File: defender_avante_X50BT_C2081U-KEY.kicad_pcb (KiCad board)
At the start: 2 copper layers, 172.7 x 61 mm, 77 parts, among them CN301 CONNECTOR_M_006_20_SPECIAL, J300 JUMPER, J301 JUMPER, J302 JUMPER, J303 JUMPER, J304 JUMPER, J305 JUMPER, J306 JUMPER, J307 JUMPER, J308 JUMPER, J309 JUMPER, J310 JUMPER, J311 JUMPER, J312 JUMPER, J313 JUMPER, J314 JUMPER, J315 JUMPER, J316 JUMPER, J317 JUMPER, J318 JUMPER, J319 JUMPER, J320 JUMPER, J321 JUMPER, J322 JUMPER, J323 JUMPER, J324 JUMPER, J325 JUMPER, J326 JUMPER, J327 JUMPER, J328 JUMPER, J329 JUMPER, J330 JUMPER, J331 JUMPER, J332 JUMPER, J333 JUMPER, J334 JUMPER, J335 JUMPER, J336 JUMPER, J337 JUMPER, Q300 BJT_NPN_GENERAL, U300 IC_X2Y_TM1668

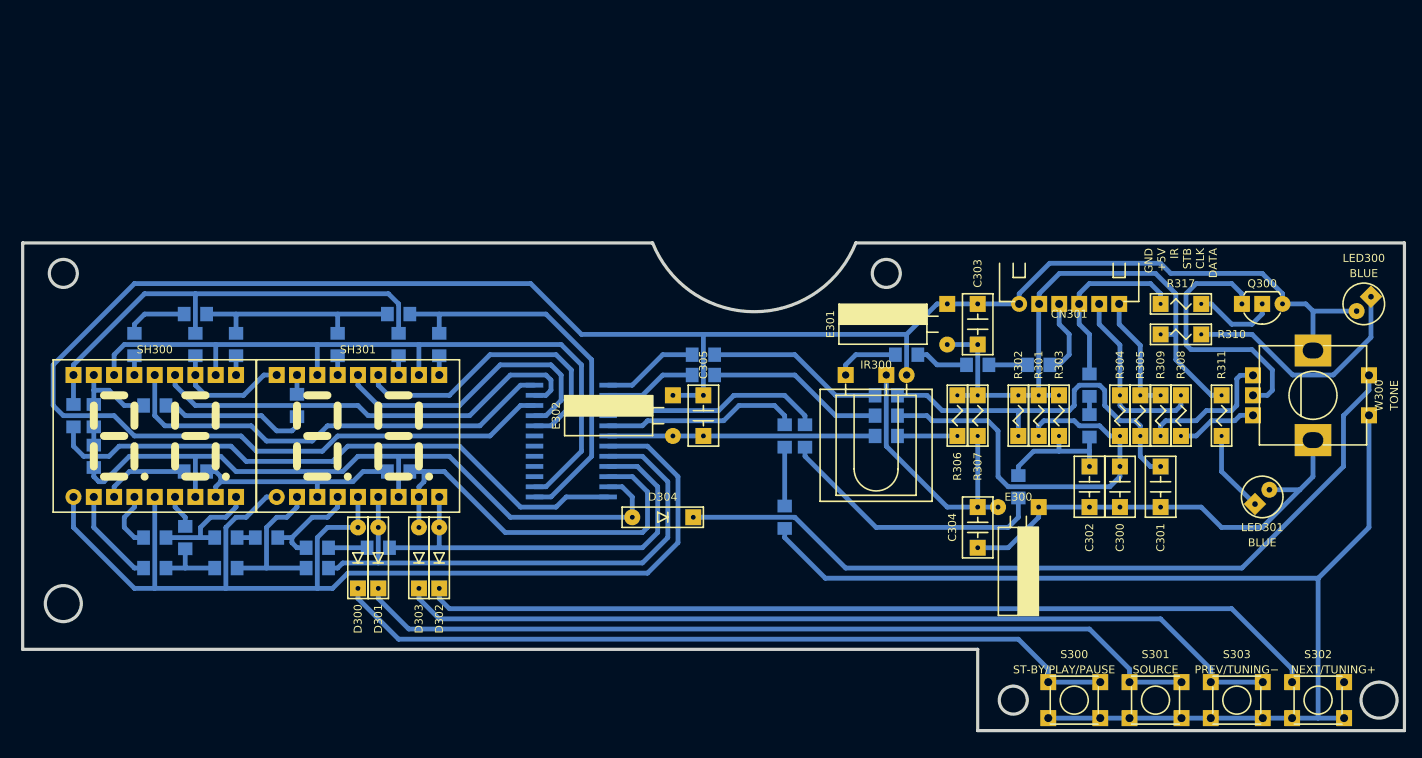
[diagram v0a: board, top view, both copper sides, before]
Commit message: Скорректированы размеры платы, положение монтажных отверстий, кнопок, энкодера и светодиодов. Заменены держатели светодиодов
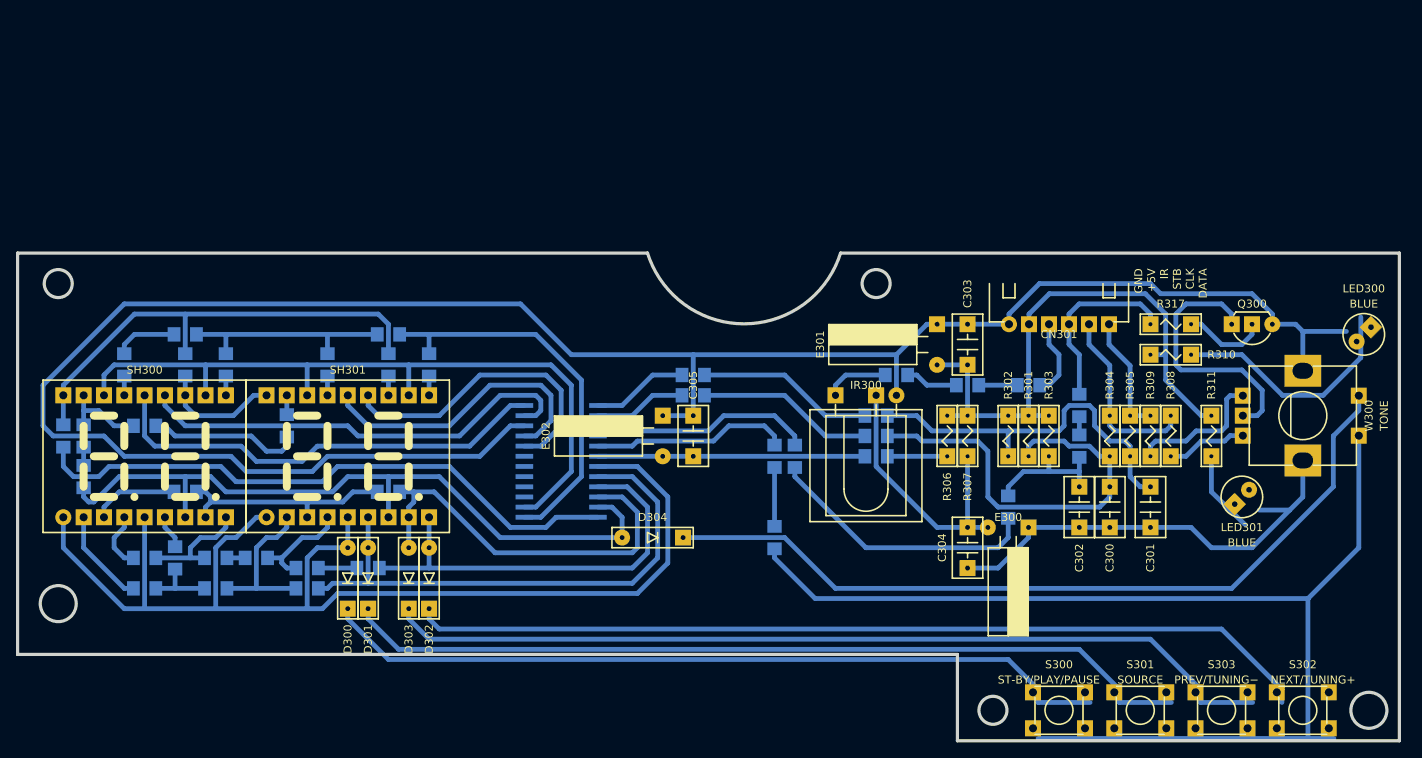
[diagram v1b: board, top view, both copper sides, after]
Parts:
- LED300, LED301: footprint KCL:LED-ROUND-03.0-UNI-SH-SPACER-HD-2.54 -> KCL:LED-ROUND-03.0-UNI-SH-SPACER
- moved LED300 3.81 mm to (229.9, 85.1)
- moved C301 2.84 mm to (203.2, 106.7)
- moved C302 2.84 mm to (194.3, 106.7)
- moved C303 2.84 mm to (180.3, 86.4)
- moved C304 2.84 mm to (180.3, 111.8)
- moved E301 2.84 mm to (176.5, 86.4)
- moved J300 2.84 mm to (194.3, 94.0)
- moved J301 2.84 mm to (194.3, 99.1)
- moved J303 2.84 mm to (185.4, 106.7)
- moved J305 2.84 mm to (171.4, 90.2)
- moved J306 2.84 mm to (168.9, 95.2)
- moved J307 2.84 mm to (168.9, 97.8)
- moved J324 2.84 mm to (87.6, 88.9)
- moved J335 2.84 mm to (69.8, 97.8)
- moved J336 2.84 mm to (69.8, 102.9)
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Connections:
- LED300 pad A: Net-(LED300-PadA) -> (no net)
- LED300 pad C: COM -> (no net)
- LED301 pad A: Net-(LED301-PadA) -> (no net)
- LED301 pad C: COM -> (no net)
- S300 pad 1COM: Net-(D300-PadC) -> (no net)
- S300 pad 1NO: /K2 -> (no net)
- S301 pad 1COM: Net-(D301-PadC) -> (no net)
- S301 pad 1NO: /K2 -> (no net)
- S302 pad 1COM: Net-(D302-PadC) -> (no net)
- S302 pad 1NO: /K2 -> (no net)
- S303 pad 1COM: Net-(D303-PadC) -> (no net)
- S303 pad 1NO: /K2 -> (no net)
- W300 pad 0: COM -> (no net)
- W300 pad A: Net-(R309-Pad1) -> (no net)
- W300 pad B: Net-(R308-Pad1) -> (no net)
- W300 pad C: Net-(Q300-PadC) -> (no net)
- W300 pad COM: Net-(D304-PadC) -> (no net)
- W300 pad NO: /K2 -> (no net)
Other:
- outline, holes or cut-outs redrawn

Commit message: Положение элементов и печатных дорожек скорректировано с учётом новых размеров платы
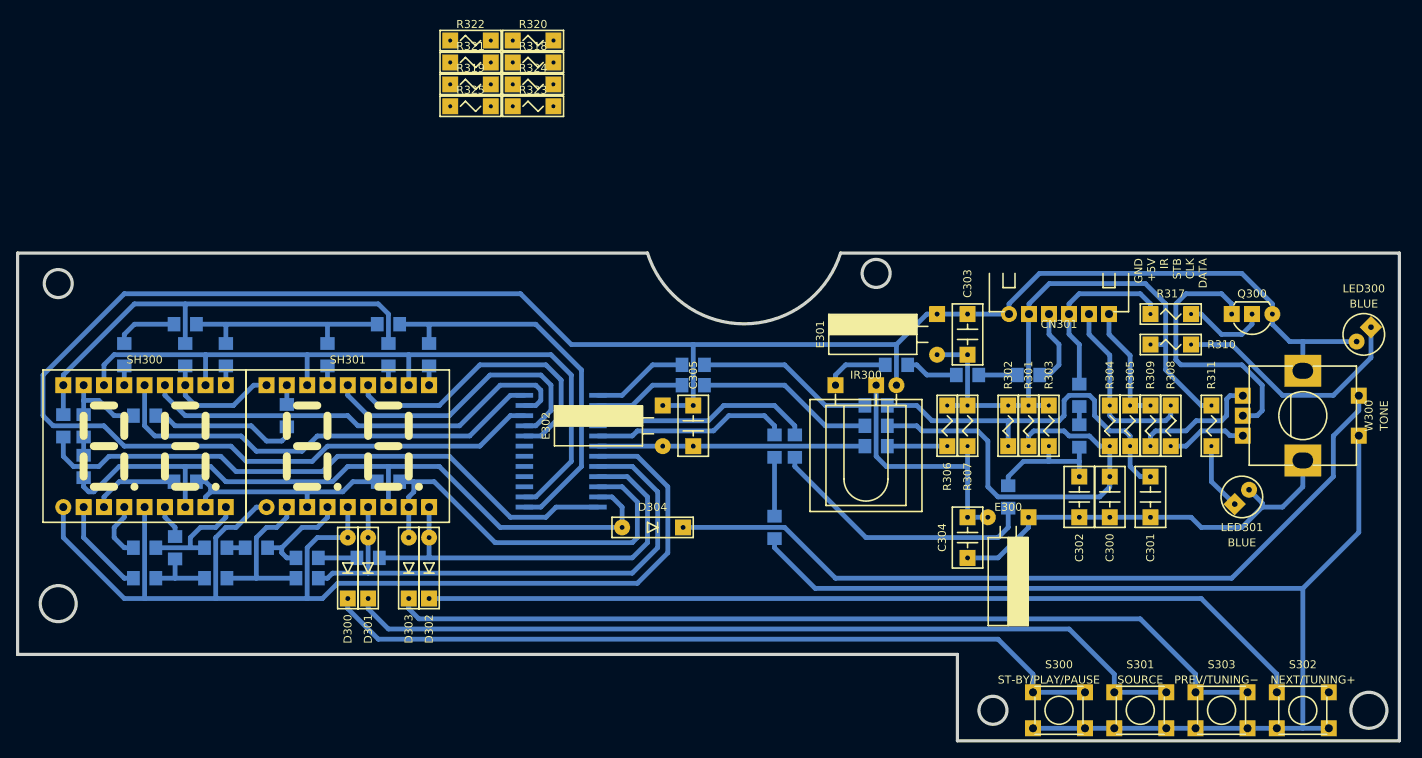
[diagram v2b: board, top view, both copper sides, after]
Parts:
- added R318: RESISTOR_GENERAL, KCL:R-MFR-12, F.Cu at (126.0, 51.1)
- added R319: RESISTOR_GENERAL, KCL:R-MFR-12, F.Cu at (118.2, 53.8)
- added R320: RESISTOR_GENERAL, KCL:R-MFR-12, F.Cu at (126.0, 48.4)
- added R321: RESISTOR_GENERAL, KCL:R-MFR-12, F.Cu at (118.2, 51.1)
- added R322: RESISTOR_GENERAL, KCL:R-MFR-12, F.Cu at (118.2, 48.4)
- added R323: RESISTOR_GENERAL, KCL:R-MFR-12, F.Cu at (126.0, 56.6)
- added R324: RESISTOR_GENERAL, KCL:R-MFR-12, F.Cu at (126.0, 53.8)
- added R325: RESISTOR_GENERAL, KCL:R-MFR-12, F.Cu at (118.2, 56.6)
- moved C300 1.27 mm to (198.1, 105.4)
- moved C301 1.27 mm to (203.2, 105.4)
- moved C302 1.27 mm to (194.3, 105.4)
- moved C304 1.27 mm to (180.3, 110.5)
- moved C305 1.27 mm to (146.1, 96.5)
- moved E302 1.27 mm to (142.2, 96.5)
- moved J300 1.27 mm to (194.3, 92.7)
- moved J303 1.27 mm to (185.4, 105.4)
- moved J307 1.27 mm to (168.9, 96.5)
- moved J314 1.27 mm to (113.0, 87.6)
- moved J315 1.27 mm to (108.0, 83.8)
- moved J316 1.27 mm to (108.0, 87.6)
- moved J317 1.27 mm to (108.0, 103.5)
- moved J319 1.27 mm to (100.3, 87.6)
- moved J321 1.27 mm to (97.8, 115.6)
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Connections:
- LED300 pad A: (no net) -> Net-(LED300-PadA)
- LED300 pad C: (no net) -> COM
- LED301 pad A: (no net) -> Net-(LED301-PadA)
- LED301 pad C: (no net) -> COM
- S300 pad 1COM: (no net) -> Net-(D300-PadC)
- S300 pad 1NO: (no net) -> /K2
- S301 pad 1COM: (no net) -> Net-(D301-PadC)
- S301 pad 1NO: (no net) -> /K2
- S302 pad 1COM: (no net) -> Net-(D302-PadC)
- S302 pad 1NO: (no net) -> /K2
- S303 pad 1COM: (no net) -> Net-(D303-PadC)
- S303 pad 1NO: (no net) -> /K2
- U300 pad 10: /C -> Net-(R321-Pad1)
- U300 pad 11: /G -> Net-(R322-Pad1)
- U300 pad 12: /F -> Net-(R323-Pad1)
- U300 pad 13: /B -> Net-(R324-Pad1)
- U300 pad 14: /A -> Net-(R325-Pad1)
- U300 pad 7: /E -> Net-(R318-Pad1)
- U300 pad 8: /D -> Net-(R319-Pad1)
- U300 pad 9: /DP -> Net-(R320-Pad1)
- W300 pad 0: (no net) -> COM
- W300 pad A: (no net) -> Net-(R309-Pad1)
- W300 pad B: (no net) -> Net-(R308-Pad1)
- W300 pad C: (no net) -> Net-(Q300-PadC)
- W300 pad COM: (no net) -> Net-(D304-PadC)
- W300 pad NO: (no net) -> /K2
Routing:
- net Net-(C304-Pad1): track 34.9 -> 32.3 mm
- net Net-(LED301-PadA): track 10.3 -> 8.49 mm
- net /K2: track 179.5 -> 177.9 mm
- net COM: track 325.7 -> 324.2 mm
- net Net-(D304-PadC): track 101.9 -> 100.6 mm
- net Net-(Q300-PadC): track 33.0 -> 34.3 mm
- net Net-(R309-Pad1): track 17.4 -> 16.1 mm
- net Net-(D302-PadC): track 113.2 -> 112.2 mm
- net Net-(LED300-PadA): track 30.4 -> 30.9 mm
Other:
- outline, holes or cut-outs redrawn

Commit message: Обновлено УГО ИМС
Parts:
- U300: value IC_X2Y_TM1668 -> TM1668
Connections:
- U300 pad 1: /IC_DATA -> Net-(U300-Pad1)
- U300 pad 10: Net-(R321-Pad1) -> Net-(U300-Pad10)
- U300 pad 11: Net-(R322-Pad1) -> Net-(U300-Pad11)
- U300 pad 12: Net-(R323-Pad1) -> Net-(U300-Pad12)
- U300 pad 13: Net-(R324-Pad1) -> Net-(U300-Pad13)
- U300 pad 14: Net-(R325-Pad1) -> Net-(U300-Pad14)
- U300 pad 2: /IC_CLK -> Net-(U300-Pad2)
- U300 pad 20: /DIG4 -> Net-(U300-Pad20)
- U300 pad 21: /DIG3 -> Net-(U300-Pad21)
- U300 pad 22: COM -> Net-(U300-Pad22)
- U300 pad 23: /DIG2 -> Net-(U300-Pad23)
- U300 pad 24: /DIG1 -> Net-(U300-Pad24)
- U300 pad 3: /STB -> Net-(U300-Pad3)
- U300 pad 5: /K2 -> Net-(U300-Pad5)
- U300 pad 6: /IC_+5V -> Net-(U300-Pad6)
- U300 pad 7: Net-(R318-Pad1) -> Net-(U300-Pad7)
- U300 pad 8: Net-(R319-Pad1) -> Net-(U300-Pad8)
- U300 pad 9: Net-(R320-Pad1) -> Net-(U300-Pad9)
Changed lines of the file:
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@@
     (zones 0)
     (modules 85)
-    (nets 49)
+    (nets 67)
   )
   (page A4)
   (title_block
     (title defender_avante_X50BT_C2081U-KEY)
-    (date 2019-04-24)
+    (date 2019-04-25)
     (rev 2)
     (company "Igor Vladimirovich Ivanov")
@@
   (net 47 "Net-(R324-Pad1)")
   (net 48 "Net-(R323-Pad1)")
+  (net 49 "Net-(U300-Pad20)")
+  (net 50 "Net-(U300-Pad14)")
+  (net 51 "Net-(U300-Pad13)")
+  (net 52 "Net-(U300-Pad12)")
+  (net 53 "Net-(U300-Pad11)")
+  (net 54 "Net-(U300-Pad10)")
+  (net 55 "Net-(U300-Pad9)")
+  (net 56 "Net-(U300-Pad8)")
+  (net 57 "Net-(U300-Pad7)")
+  (net 58 "Net-(U300-Pad6)")
+  (net 59 "Net-(U300-Pad5)")
+  (net 60 "Net-(U300-Pad24)")
+  (net 61 "Net-(U300-Pad23)")
+  (net 62 "Net-(U300-Pad22)")
+  (net 63 "Net-(U300-Pad21)")
+  (net 64 "Net-(U300-Pad3)")
+  (net 65 "Net-(U300-Pad2)")
+  (net 66 "Net-(U300-Pad1)")
   (net_class Default "This is the default net class."
     (clearance 0)
@@
     (add_net "Net-(R324-Pad1)")
     (add_net "Net-(R325-Pad1)")
+    (add_net "Net-(U300-Pad1)")
+    (add_net "Net-(U300-Pad10)")
+    (add_net "Net-(U300-Pad11)")
+    (add_net "Net-(U300-Pad12)")
+    (add_net "Net-(U300-Pad13)")
+    (add_net "Net-(U300-Pad14)")
     (add_net "Net-(U300-Pad15)")
     (add_net "Net-(U300-Pad16)")
@@
     (add_net "Net-(U300-Pad18)")
     (add_net "Net-(U300-Pad19)")
+    (add_net "Net-(U300-Pad2)")
+    (add_net "Net-(U300-Pad20)")
+    (add_net "Net-(U300-Pad21)")
+    (add_net "Net-(U300-Pad22)")
+    (add_net "Net-(U300-Pad23)")
+    (add_net "Net-(U300-Pad24)")
+    (add_net "Net-(U300-Pad3)")
     (add_net "Net-(U300-Pad4)")
+    (add_net "Net-(U300-Pad5)")
+    (add_net "Net-(U300-Pad6)")
+    (add_net "Net-(U300-Pad7)")
+    (add_net "Net-(U300-Pad8)")
+    (add_net "Net-(U300-Pad9)")
     (add_net V)
   )
@@
       (effects (font (size 1 1) (thickness 0.2)) (justify mirror))
     )
-    (fp_text value IC_X2Y_TM1668 (at 0 10.16 180) (layer B.Fab) hide
+    (fp_text value TM1668 (at 0 10.16 180) (layer B.Fab) hide
       (effects (font (size 1 1) (thickness 0.2)) (justify mirror))
     )
@@
       (net 34 "Net-(U300-Pad18)"))
     (pad 20 smd rect (at 4.6 1.905 180) (size 2.2 0.6) (layers B.Cu B.Mask)
-      (net 22 /DIG4))
+      (net 49 "Net-(U300-Pad20)"))
     (pad 17 smd rect (at 4.6 -1.905 180) (size 2.2 0.6) (layers B.Cu B.Mask)
       (net 33 "Net-(U300-Pad17)"))
@@
       (net 32 "Net-(U300-Pad15)"))
     (pad 14 smd rect (at 4.6 -5.715 180) (size 2.2 0.6) (layers B.Cu B.Mask)
-      (net 46 "Net-(R325-Pad1)"))
+      (net 50 "Net-(U300-Pad14)"))
     (pad 19 smd rect (at 4.6 0.635 180) (size 2.2 0.6) (layers B.Cu B.Mask)
       (net 31 "Net-(U300-Pad19)"))
@@
       (net 30 "Net-(U300-Pad16)"))
     (pad 13 smd rect (at 4.6 -6.985 180) (size 2.2 0.6) (layers B.Cu B.Mask)
-      (net 47 "Net-(R324-Pad1)"))
+      (net 51 "Net-(U300-Pad13)"))
     (pad 12 smd rect (at -4.6 -6.985 180) (size 2.2 0.6) (layers B.Cu B.Mask)
-      (net 48 "Net-(R323-Pad1)"))
+      (net 52 "Net-(U300-Pad12)"))
     (pad 11 smd rect (at -4.6 -5.715 180) (size 2.2 0.6) (layers B.Cu B.Mask)
-      (net 41 "Net-(R322-Pad1)"))
+      (net 53 "Net-(U300-Pad11)"))
     (pad 10 smd rect (at -4.6 -4.445 180) (size 2.2 0.6) (layers B.Cu B.Mask)
-      (net 42 "Net-(R321-Pad1)"))
+      (net 54 "Net-(U300-Pad10)"))
     (pad 9 smd rect (at -4.6 -3.175 180) (size 2.2 0.6) (layers B.Cu B.Mask)
-      (net 43 "Net-(R320-Pad1)"))
+      (net 55 "Net-(U300-Pad9)"))
     (pad 8 smd rect (at -4.6 -1.905 180) (size 2.2 0.6) (layers B.Cu B.Mask)
-      (net 44 "Net-(R319-Pad1)"))
+      (net 56 "Net-(U300-Pad8)"))
     (pad 7 smd rect (at -4.6 -0.635 180) (size 2.2 0.6) (layers B.Cu B.Mask)
-      (net 45 "Net-(R318-Pad1)"))
+      (net 57 "Net-(U300-Pad7)"))
     (pad 6 smd rect (at -4.6 0.635 180) (size 2.2 0.6) (layers B.Cu B.Mask)
-      (net 36 /IC_+5V))
+      (net 58 "Net-(U300-Pad6)"))
     (pad 5 smd rect (at -4.6 1.905 180) (size 2.2 0.6) (layers B.Cu B.Mask)
-      (net 24 /K2))
+      (net 59 "Net-(U300-Pad5)"))
     (pad 24 smd rect (at 4.6 6.985 180) (size 2.2 0.6) (layers B.Cu B.Mask)
-      (net 20 /DIG1))
+      (net 60 "Net-(U300-Pad24)"))
     (pad 23 smd rect (at 4.6 5.715 180) (size 2.2 0.6) (layers B.Cu B.Mask)
-      (net 19 /DIG2))
+      (net 61 "Net-(U300-Pad23)"))
     (pad 22 smd rect (at 4.6 4.445 180) (size 2.2 0.6) (layers B.Cu B.Mask)
-      (net 40 COM))
+      (net 62 "Net-(U300-Pad22)"))
     (pad 21 smd rect (at 4.6 3.175 180) (size 2.2 0.6) (layers B.Cu B.Mask)
-      (net 21 /DIG3))
+      (net 63 "Net-(U300-Pad21)"))
     (pad 4 smd rect (at -4.6 3.175 180) (size 2.2 0.6) (layers B.Cu B.Mask)
       (net 29 "Net-(U300-Pad4)"))
     (pad 3 smd rect (at -4.6 4.445 180) (size 2.2 0.6) (layers B.Cu B.Mask)
-      (net 9 /STB))
+      (net 64 "Net-(U300-Pad3)"))
     (pad 2 smd rect (at -4.6 5.715 180) (size 2.2 0.6) (layers B.Cu B.Mask)
-      (net 38 /IC_CLK))
+      (net 65 "Net-(U300-Pad2)"))
     (pad 1 smd rect (at -4.6 6.985 180) (size 2.2 0.6) (layers B.Cu B.Mask)
-      (net 37 /IC_DATA))
+      (net 66 "Net-(U300-Pad1)"))
   )
   (module KCL:J-SMD-1206 (layer B.Cu)
@@
       (net 27 "Net-(D303-PadC)"))
   )
-  (module KCL:ENC-PEC12R-4-F-S locked (layer F.Cu)
+  (module KCL:ENC-PEC12R-4-F-S (layer F.Cu)
     (at 222.25 95.25 270)
     (fp_text reference W300 (at 0 -8.255 90) (layer F.SilkS)
